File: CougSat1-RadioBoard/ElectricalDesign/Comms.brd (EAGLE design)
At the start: 90.4 x 95.8 mm, 411 parts, among them J1 230mm Antenna, J2 CougSat Card, J3 700mm Antenna, J4 SWD, Q1 CSD25402Q3A, Q12 DMN53D0LDW, Q2 CSD25402Q3A, Q3 DMN53D0LDW, Q9 DMN53D0LDW, U1 INA199C1, U10 HMC452QS16G, U11 AD8515, U12 AD7291, U13 AD8515, U14 LP5907MFX-3.1, U15 AD9761, U16 TXS0102DQM, U18 TXS0102DQM, U19 MMZ09332B, U2 LP5907MFX-3.1, U20 ADF4360, U21 HMC545A, U22 AD9761, U23 MAAM-011229, U24 AD8515, U25 MAAM-011229, U26 AD8345, U28 AD8348, U29 AD7291, U3 TPS61236, U30 TXS0102DQM, U31 MAAM-011229, U32 AD8515, U35 TXS0102DQM, U36 ADF4360, U37 MAAM-011229, U39 AD8515, U4 AD8346, U40 AD8515, U42 TXS0102DQM, U43 INA199C2, U44 TXS0102DQM, U45 TXS0102DQM, U46 TXS0102DQM, U47 TXS0102DQM, U48 AD7291, U49 AD8515, U5 ADF4360, U50 INA199C2, U51 LP5907MFX-3.1, U52 INA199C2, U53 INA199C1, U54 TXS0102DQM, U55 TXS0102DQM, U6 STM32L496VGT, U7 GRF2133, U8 IS25LP016D, U9 IS25LP016D, Y1 19.68MHz ±2.5ppm, Y2 8MHz ±10ppm, Y3 32.768kHz ±10ppm, Y4 19.68MHz ±2.5ppm, Y5 19.68MHz ±2.5ppm

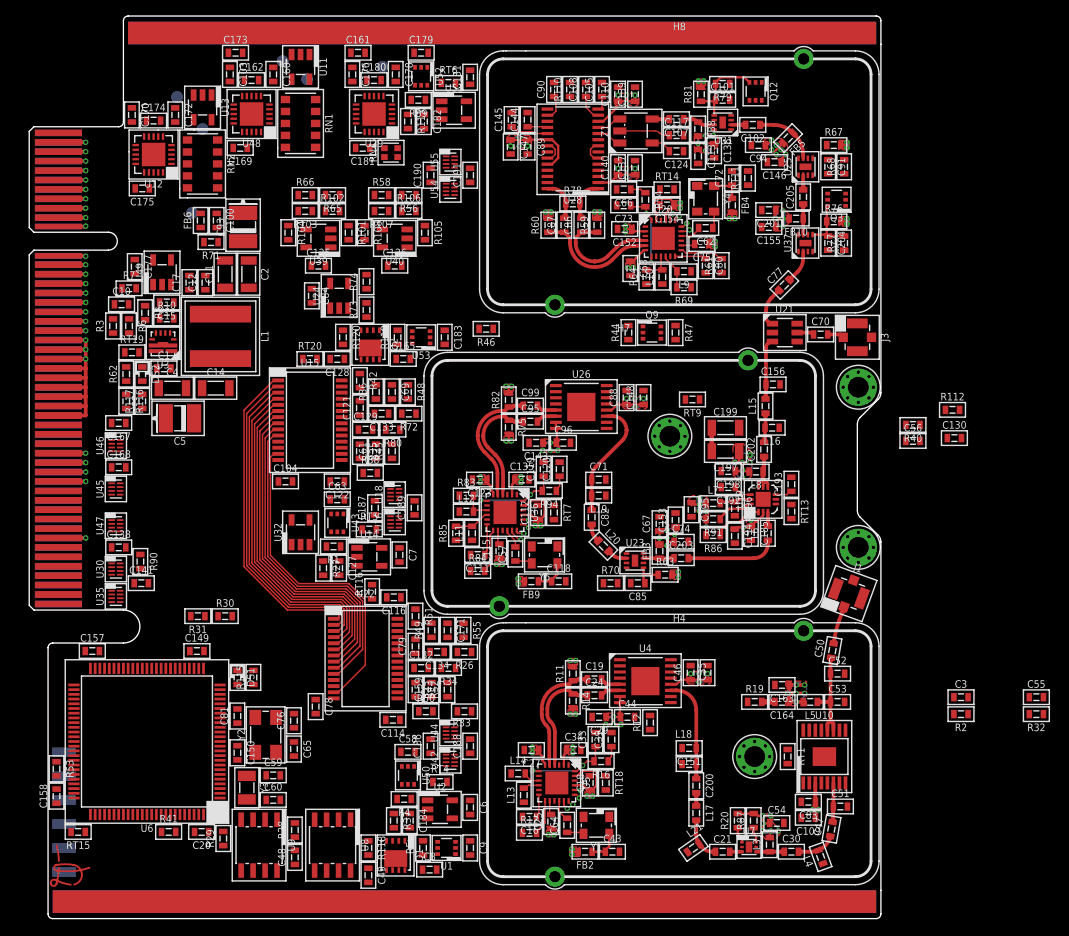
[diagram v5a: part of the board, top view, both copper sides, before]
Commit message: Changed isolated ground to a solid DGND and relaying on layout to ensure good layout
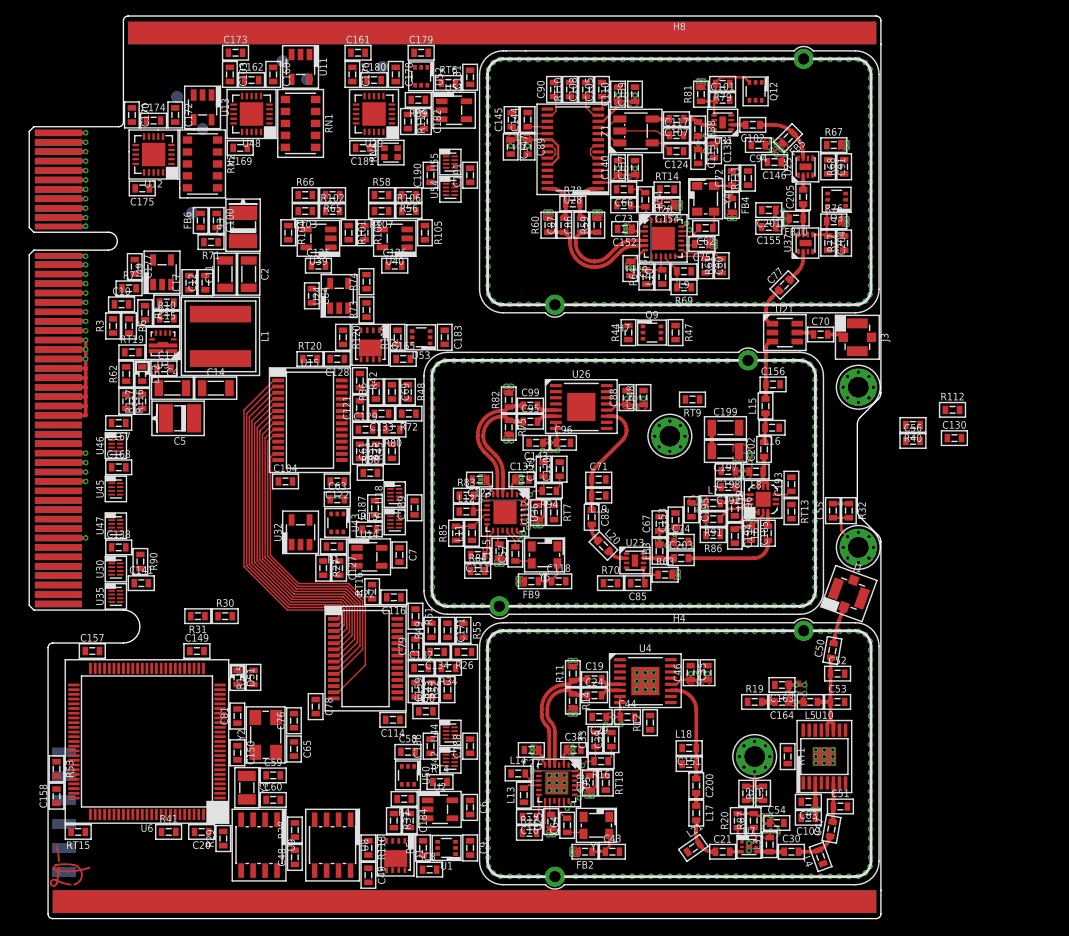
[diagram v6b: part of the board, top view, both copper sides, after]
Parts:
- removed R33, R46: 0Ω <20mΩ, CougsInSpace-Resistors:1608
- moved R32 29.4 mm to (87.0, -4.60), turned to 270 degrees
- moved C55 29.3 mm to (85.3, -4.60), turned to 90 degrees
- moved C3 25.0 mm to (76.1, -34.6), turned to 270 degrees
- moved R2 22.6 mm to (77.9, -34.6), turned to 90 degrees
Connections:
- removed net RFGND-0: C109.2, C114.2, C116.2, C132.2, C151.2, C16.2, C163.2, C18.2, C27.2, C33.2, C34.2, C39.2, C43.2, C51.2, C52.2, C53.2, C54.2, C79.2, C83.2, H4.1, H4.2, J1.SHIELD@1, J1.SHIELD@13, J1.SHIELD@2, L13.1, L14.1, L18.1, L21.1, L4.1, R12.1, R19.1, R26.1, R33.1, R50.1, R51.1, R52.1, R55.1, U10.1, U10.10, U10.13, U10.14, U10.15, U10.16, U10.2, U10.4, U10.5, U10.7, U10.8, U10.9, U10.PAD, U22.19, U22.24, U4.10, U4.13, U4.14, U4.3, U4.4, U4.9, U4.PAD, U5.1, U5.11, U5.15, U5.22, U5.3, U5.8, U5.PAD, U7.2, U7.5, U7.PAD, Y1.2
- new net N$7: L12.1, R83.1
- net DGND: now also C101.2, C105.2, C108.2, C109.2, C110.2, C111.2, C112.2, C113.2, C114.2, C116.2, C117.2, C118.2, C119.2, C120.2, C121.2, C122.2, C123.2, C124.1, C128.2, C129.2, C130.2, C132.2, C135.2, C136.2, C137.2, C139.2, C140.2, C143.2, C144.2, C145.2, C146.2, C147.2, C148.2, C151.2, C152.2, C153.2, C154.2, C155.2, C156.2, C16.2, C163.2, C18.2, C185.2, C188.2, C189.2, C191.2, C192.2, C194.2, C195.2, C196.2, C198.2, C199.2, C201.2, C204.2, C27.2, C29.2, C3.2, C33.2, C34.2, C35.2, C39.2, C43.2, C44.2, C46.2, C51.2, C52.2, C53.2, C54.2, C55.2, C56.2, C66.2, C67.2, C68.2, C71.2, C72.2, C73.2, C74.2, C79.2, C80.2, C83.2, C85.2, C88.2, C89.2, C90.2, C91.2, C94.2, C96.2, H4.1, H4.2, H7.1, H7.2, H8.1, H8.2, J1.SHIELD@1, J1.SHIELD@13, J1.SHIELD@2, J3.SHIELD@1, J3.SHIELD@13, J3.SHIELD@2, L10.1, L11.1, L13.1, L14.1, L16.1, L18.1, L19.1, L21.1, L4.1, L9.1, Q12.1, Q12.4, Q3.1, Q3.3, Q3.4, Q3.5, Q9.1, Q9.4, R112.1, R12.1, R19.1, R2.1, R26.1, R32.1, R38.1, R40.1, R42.1, R45.1, R48.1, R50.1, R51.1, R52.1, R55.1, R61.1, R64.1, R68.1, R69.1, R70.1, R72.1, R77.1, R79.1, R84.1, R85.1, U10.1, U10.10, U10.13, U10.14, U10.15, U10.16, U10.2, U10.4, U10.5, U10.7, U10.8, U10.9, U10.PAD, U15.19, U15.24, U20.1, U20.11, U20.15, U20.22, U20.3, U20.8, U20.PAD, U21.2, U22.19, U22.24, U23.1, U23.3, U23.4, U23.6, U23.8, U23.PAD, U25.1, U25.3, U25.4, U25.6, U25.8, U25.PAD, U26.10, U26.13, U26.14, U26.3, U26.4, U26.9, U26.PAD, U28.22, U28.27, U28.7, U28.9, U31.1, U31.3, U31.4, U31.6, U31.8, U31.PAD, U36.1, U36.11, U36.15, U36.22, U36.3, U36.8, U36.PAD, U37.1, U37.3, U37.4, U37.6, U37.8, U37.PAD, U4.10, U4.13, U4.14, U4.3, U4.4, U4.9, U4.PAD, U5.1, U5.11, U5.15, U5.22, U5.3, U5.8, U5.PAD, U7.2, U7.5, U7.PAD, Y1.2, Y4.2, Y5.2; no longer R33.2, R46.2
- net PGND: no longer C130.2, C3.2, C55.2, C56.2, Q9.1, Q9.4, R112.1, R2.1, R32.1, R40.1
- net RFGND-1: no longer C101.2, C105.2, C108.2, C110.2, C111.2, C112.2, C113.2, C117.2, C118.2, C119.2, C120.2, C121.2, C122.2, C123.2, C124.1, C128.2, C129.2, C135.2, C136.2, C137.2, C139.2, C140.2, C143.2, C144.2, C145.2, C146.2, C147.2, C148.2, C152.2, C153.2, C154.2, C155.2, C156.2, C185.2, C188.2, C189.2, C191.2, C192.2, C194.2, C195.2, C196.2, C198.2, C199.2, C201.2, C204.2, C29.2, C35.2, C44.2, C46.2, C66.2, C67.2, C68.2, C71.2, C72.2, C73.2, C74.2, C80.2, C85.2, C88.2, C89.2, C90.2, C91.2, C94.2, C96.2, H7.1, H7.2, H8.1, H8.2, J3.SHIELD@1, J3.SHIELD@13, J3.SHIELD@2, L10.1, L11.1, L12.1, L16.1, L19.1, L9.1, Q12.1, Q12.4, Q3.1, Q3.3, Q3.4, Q3.5, R38.1, R42.1, R45.1, R46.1, R48.1, R61.1, R64.1, R68.1, R69.1, R70.1, R72.1, R77.1, R79.1, R83.1, R84.1, R85.1, U15.19, U15.24, U20.1, U20.11, U20.15, U20.22, U20.3, U20.8, U20.PAD, U21.2, U23.1, U23.3, U23.4, U23.6, U23.8, U23.PAD, U25.1, U25.3, U25.4, U25.6, U25.8, U25.PAD, U26.10, U26.13, U26.14, U26.3, U26.4, U26.9, U26.PAD, U28.22, U28.27, U28.7, U28.9, U31.1, U31.3, U31.4, U31.6, U31.8, U31.PAD, U36.1, U36.11, U36.15, U36.22, U36.3, U36.8, U36.PAD, U37.1, U37.3, U37.4, U37.6, U37.8, U37.PAD, Y4.2, Y5.2
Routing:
- net CHASSIS_230-0: track 0.00 -> 16.8 mm
- net CHASSIS_230-1: track 0.00 -> 16.2 mm
- net 3.3V_0: track 0.00 -> 5.80 mm, vias 0 -> 1
- net DGND: track 0.00 -> 3.50 mm, vias 0 -> 94
- added copper zone on layer 15, net CHASSIS_230-0
- added copper zone on layer 2, net CHASSIS_230-0
- added copper zone on layer 15, net CHASSIS_230-1
- added copper zone on layer 2, net CHASSIS_230-1
- added copper zone on layer 2, net DGND

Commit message: Laid out 230mm radio
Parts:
- moved FB2 6.72 mm to (63.2, -35.6), turned to 90 degrees
- moved C43 2.67 mm to (63.2, -38.5), turned to 270 degrees
- moved RT1 2.33 mm to (80.1, -33.0)
- moved C8 0.92 mm to (41.8, -43.3), turned to 270 degrees
- moved RT4 0.89 mm to (43.0, -34.1), turned to 180 degrees
- moved C186 0.71 mm to (42.5, -30.3)
- moved U42 0.71 mm to (44.6, -31.8)
- moved U44 0.71 mm to (44.6, -28.9)
- moved C188 0.71 mm to (46.7, -30.3)
- moved U2 0.65 mm to (43.6, -37.0)
- moved C6 0.65 mm to (46.8, -36.8)
- moved J1 0.22 mm to (87.2, -13.5)
- turned RT18 to 90 degrees
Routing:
- net DGND: track 3.50 -> 839.0 mm, vias 94 -> 617
- net 5.0V_0: track 19.5 -> 86.3 mm, vias 14 -> 19
- net 3.1V_0: track 30.8 -> 92.1 mm, vias 22 -> 27
- net AGND: track 0.00 -> 46.3 mm, vias 0 -> 2
- net TEMP_PA_230: track 0.00 -> 35.2 mm, vias 0 -> 1
- net MOD_230_QD_N: track 0.00 -> 23.2 mm, vias 0 -> 1
- net MOD_230_QD_P: track 0.00 -> 23.0 mm, vias 0 -> 1
- net TEMP_MOD_700: track 0.00 -> 21.2 mm, vias 0 -> 1
- net TEMP_CLK_230: track 0.00 -> 18.7 mm, vias 0 -> 1
- net MOD_230_ID_P: track 0.00 -> 15.4 mm, vias 0 -> 1
- net MOD_230_ID_N: track 0.00 -> 15.2 mm, vias 0 -> 1
- net MUXOUT-230: track 0.62 -> 12.3 mm
- net !230_CS: track 0.64 -> 12.0 mm
- net 230_MOSI: track 0.70 -> 11.6 mm
- net 230_SCK: track 0.94 -> 11.2 mm
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- added copper zone on layer 1, net DGND
- added copper zone on layer 15, net DGND
- added copper zone on layer 16, net DGND
- added copper zone on layer 1, net MOD_LNA_230_RFIN

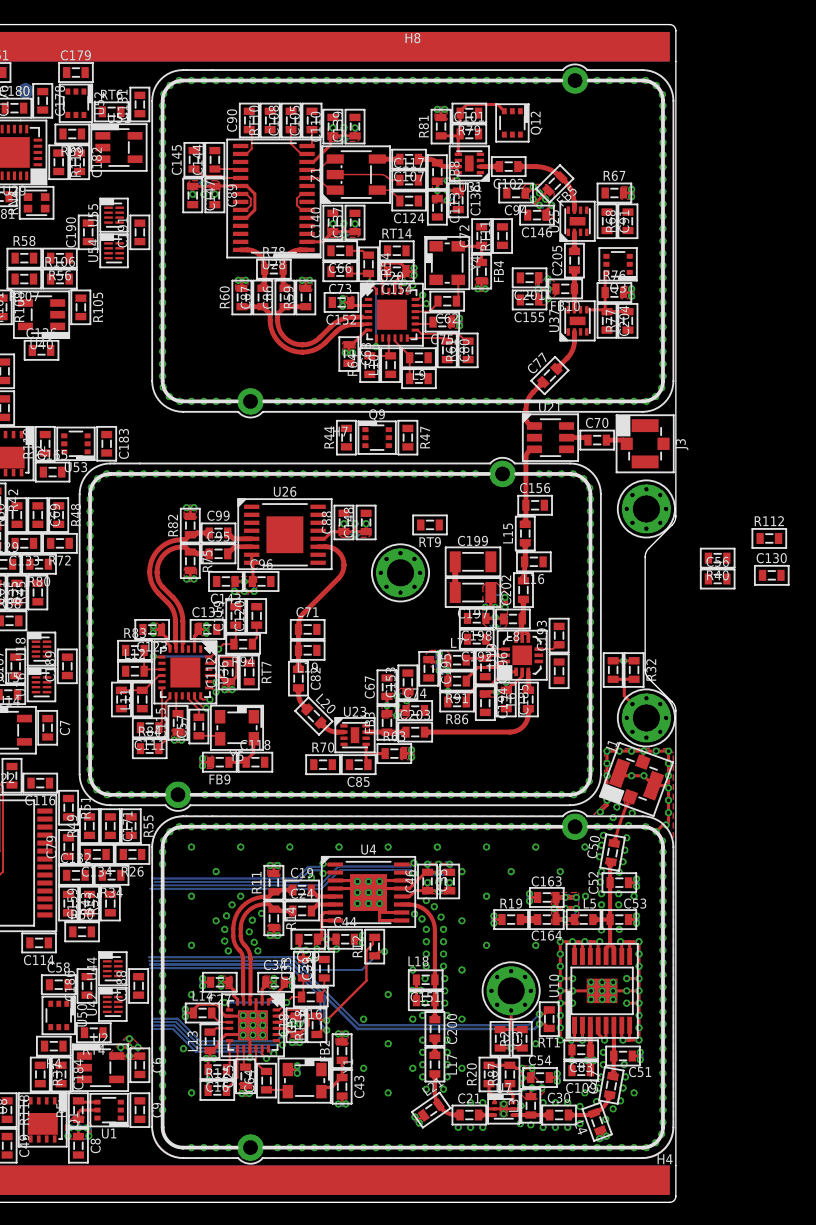
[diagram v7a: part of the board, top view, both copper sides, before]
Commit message: Laid out 700mm modulator
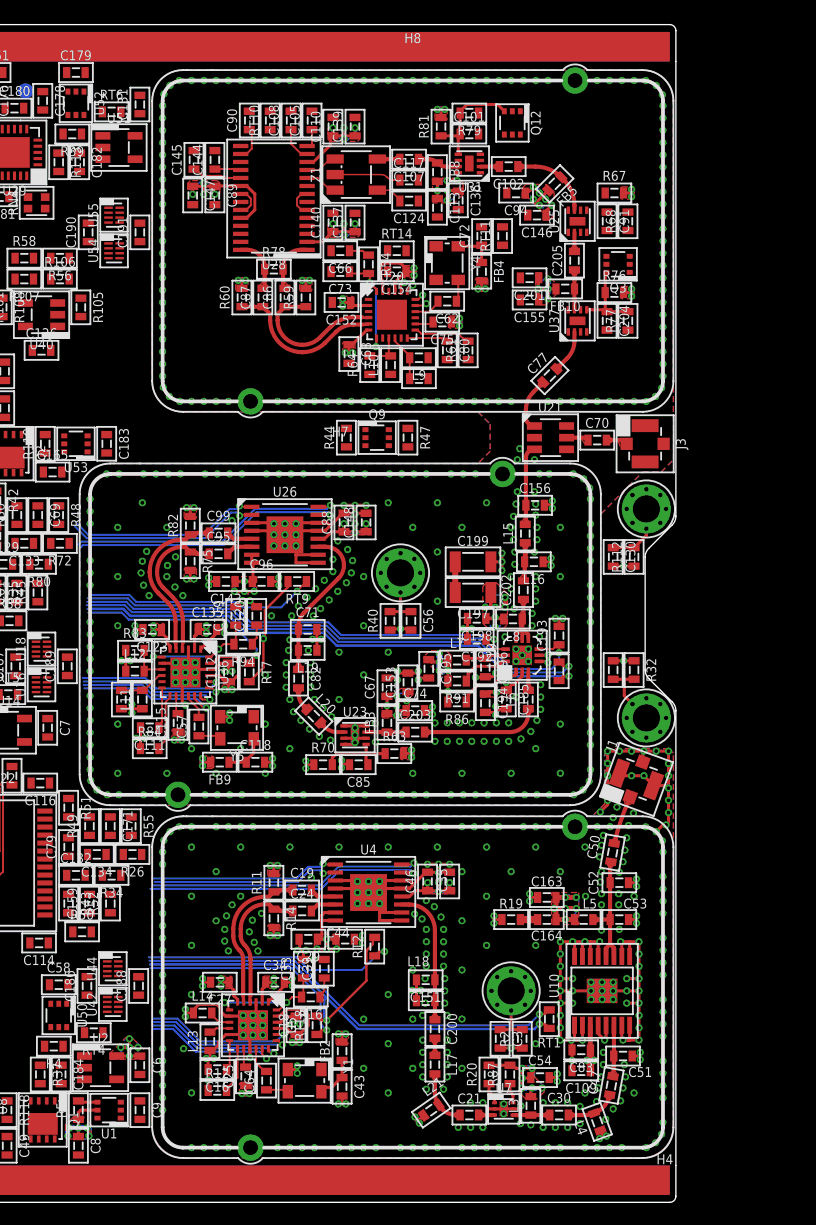
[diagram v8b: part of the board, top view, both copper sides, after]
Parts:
- moved R40 27.1 mm to (67.2, -0.60), turned to 90 degrees
- moved C56 25.2 mm to (68.8, -0.60), turned to 270 degrees
- moved C130 13.0 mm to (85.3, 4.60), turned to 270 degrees
- moved RT9 11.7 mm to (59.6, 2.60)
- moved R112 11.1 mm to (87.0, 4.60), turned to 90 degrees
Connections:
- removed net N$7: L12.1, R83.1
- removed net RFGND-1: C193.2, U19.4, U19.5, U19.PAD
- net DGND: now also C193.2, L12.1, R83.1, U19.4, U19.5, U19.PAD
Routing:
- net DGND: track 839.0 -> 1225.2 mm, vias 617 -> 789
- net 3.1V_1: track 39.1 -> 116.8 mm
- net AGND: track 46.3 -> 98.6 mm, vias 2 -> 4
- net 5.0V_1: track 17.8 -> 68.1 mm
- net TEMP_PA_700: track 0.00 -> 42.6 mm, vias 0 -> 1
- net PA_PDET_UNBUF-700: track 1.79 -> 44.1 mm, vias 0 -> 1
- net PA_PD-700: track 2.02 -> 37.1 mm, vias 0 -> 1
- net MOD_700_QD_P: track 0.00 -> 22.9 mm, vias 0 -> 1
- net MOD_700_QD_N: track 0.00 -> 22.8 mm, vias 0 -> 1
- net TEMP_MOD_230: track 0.00 -> 19.0 mm, vias 0 -> 1
- net CHASSIS_700-0: track 0.00 -> 16.5 mm
- net TEMP_CLK_MOD: track 0.00 -> 16.3 mm, vias 0 -> 1
- net CHASSIS_700-1: track 0.00 -> 16.1 mm
- net MOD_700_ID_N: track 0.00 -> 15.8 mm, vias 0 -> 1
- net MOD_700_ID_P: track 0.00 -> 15.6 mm, vias 0 -> 1
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- added copper zone on layer 15, net 3.1V_0
- added copper zone on layer 15, net 3.1V_1
- added copper zone on layer 15, net 5.0V_0
- added copper zone on layer 15, net 5.0V_1
- added copper zone on layer 1, net ANTENNA_700
- added copper zone on layer 1, net ANTENNA_700_COAX
- added copper zone on layer 15, net CHASSIS_700-0
- added copper zone on layer 2, net CHASSIS_700-0
- added copper zone on layer 15, net CHASSIS_700-1
- added copper zone on layer 2, net CHASSIS_700-1
